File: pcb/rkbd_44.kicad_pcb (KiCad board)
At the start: 2 copper layers, 104 parts, among them SW1 SW_Push, U1 ATmega32U4-AU, Y1 16MHz

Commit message: footprint layout
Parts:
- C1, C2, D1, D10, D11, D12, D13, D14, D15, D16, D17, D18, D19, D2, D20, D21, D22, D23, D24, D25, D26, D27, D28, D29, D3, D30, D31, D32, D33, D34, D35, D36, D37, D38, D39, D4, D40, D41, D42, D43, D44, D5, D6, D7, D8, D9, R2, R3, U1, USB1, Y1: moved to B.Cu
- moved D38 245.2 mm to (276.2, 114.3)
- moved MX38 227.4 mm to (269.1, 107.2)
- moved D25 225.6 mm to (276.2, 95.2)
- moved D37 219.8 mm to (257.2, 114.3)
- moved F1 206.1 mm to (129.9, -5.09)
- moved C3 206.1 mm to (140.0, -3.07)
- moved C4 206.1 mm to (153.3, -9.42)
- moved C5 206.1 mm to (144.7, -3.07)
- moved C7 206.1 mm to (153.3, -6.47)
- moved R4 206.1 mm to (149.3, -3.07)
- moved D24 201.4 mm to (257.2, 95.2)
- moved D12 195.5 mm to (276.2, 76.2)
- moved D36 195.2 mm to (238.1, 114.3)
- moved C6 194.7 mm to (171.4, 9.53)
- moved MX35 190.0 mm to (211.9, 107.2)
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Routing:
- net col12: track 0.00 -> 138.0 mm, vias 0 -> 4
- net row2: track 0.00 -> 131.4 mm
- net row1: track 0.00 -> 131.3 mm
- net col11: track 0.00 -> 119.0 mm, vias 0 -> 4
- net row0: track 0.00 -> 105.1 mm
- net col9: track 0.00 -> 104.0 mm, vias 0 -> 6
- net col10: track 0.00 -> 99.9 mm, vias 0 -> 4
- net col8: track 0.00 -> 85.4 mm, vias 0 -> 6
- net col7: track 0.00 -> 67.0 mm, vias 0 -> 6
- net row3: track 0.00 -> 44.6 mm
- net Net-(D41-Pad2): track 0.00 -> 14.4 mm
- net Net-(D34-Pad2): track 0.00 -> 13.5 mm
- net Net-(D9-Pad2): track 0.00 -> 13.4 mm
- net Net-(D8-Pad2): track 0.00 -> 13.4 mm
- net Net-(D7-Pad2): track 0.00 -> 13.4 mm
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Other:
- board outline added: 263.3 x 90.4 mm

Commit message: change mcu position, change sw footprint
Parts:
- C3, C4, C5, C6, C7, F1, R1, R4, SW1: moved to B.Cu
- MX1, MX10, MX11, MX12, MX13, MX14, MX15, MX16, MX17, MX18, MX19, MX2, MX20, MX21, MX22, MX23, MX24, MX25, MX26, MX27, MX28, MX29, MX3, MX30, MX31, MX32, MX33, MX34, MX35, MX36, MX37, MX38, MX39, MX4, MX40, MX43, MX44, MX5, MX6, MX7, MX8, MX9: footprint MX_Only:MXOnly-1U-Hotswap -> MX_Only:MXOnly-1U-NoLED
- MX41, MX42: footprint MX_Only:MXOnly-1.25U-Hotswap -> MX_Only:MXOnly-1.25U-NoLED
- moved C7 93.3 mm to (161.0, 86.5), turned to 90 degrees
- moved C4 90.8 mm to (138.0, 80.1), turned to 90 degrees
- moved R4 88.7 mm to (139.0, 85.1)
- moved C5 80.2 mm to (163.0, 75.1), turned to 270 degrees
- moved C6 75.9 mm to (163.6, 85.1), turned to 90 degrees
- moved F1 75.5 mm to (144.0, 69.1), turned to 90 degrees
- moved C3 72.5 mm to (154.0, 68.1), turned to 90 degrees
- moved C2 28.3 mm to (165.0, 62.1), turned to 90 degrees
- moved Y1 21.7 mm to (161.0, 62.1), turned to 0 degrees
- moved C1 16.1 mm to (157.0, 62.1), turned to 270 degrees
- moved USB1 14.2 mm to (150.0, 59.5)
- moved R2 13.4 mm to (150.6, 68.1), turned to 90 degrees
- moved R3 13.3 mm to (148.6, 68.1), turned to 90 degrees
- moved R1 12.8 mm to (140.0, 68.1), turned to 270 degrees
- moved U1 7.20 mm to (152.0, 78.1), turned to 270 degrees
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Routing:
- net col7: track 67.0 -> 0.00 mm, vias 6 -> 0
- net row3: track 44.6 -> 0.00 mm
- net col8: track 85.4 -> 61.1 mm
- net Net-(D41-Pad2): track 14.4 -> 0.00 mm
- net Net-(D7-Pad2): track 13.4 -> 0.00 mm
- net Net-(D33-Pad2): track 13.4 -> 0.00 mm
- net Net-(D20-Pad2): track 13.3 -> 0.00 mm
- net col9: track 104.0 -> 91.3 mm
- net col10: track 99.9 -> 87.9 mm
- net col11: track 119.0 -> 109.0 mm
- net col12: track 138.0 -> 128.4 mm
- net row2: track 131.4 -> 125.0 mm
- net row1: track 131.3 -> 125.5 mm
- net row0: track 105.1 -> 100.9 mm
- net Net-(D37-Pad2): track 13.4 -> 16.7 mm
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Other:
- board outline removed

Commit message: add cutting line
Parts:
- moved C1 20.6 mm to (165.0, 81.1), turned to 0 degrees
- moved C6 17.0 mm to (158.0, 69.1), turned to 180 degrees
- moved Y1 15.5 mm to (165.0, 77.1), turned to 90 degrees
- moved C2 11.0 mm to (165.0, 73.1), turned to 180 degrees
- moved C4 6.12 mm to (143.4, 82.9), turned to 180 degrees
- moved C5 2.83 mm to (161.0, 73.1)
- moved C7 1.22 mm to (161.9, 85.7), turned to 0 degrees
- turned D1 to 0 degrees
- turned D13 to 0 degrees
- turned D14 to 0 degrees
- turned D15 to 0 degrees
- turned D16 to 0 degrees
- turned D17 to 0 degrees
- turned D18 to 0 degrees
- turned D2 to 0 degrees
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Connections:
- U1 pad 18: Net-(U1-Pad18) -> row0
- U1 pad 19: Net-(U1-Pad19) -> col12
- U1 pad 20: Net-(U1-Pad20) -> col11
- U1 pad 21: Net-(U1-Pad21) -> col10
- U1 pad 22: Net-(U1-Pad22) -> col9
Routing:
- net row3: track 0.00 -> 108.6 mm
- net GND: track 0.00 -> 93.1 mm
- net col7: track 0.00 -> 62.1 mm, vias 0 -> 6
- net +5V: track 0.00 -> 34.6 mm
- net Net-(R1-Pad1): track 0.00 -> 31.9 mm, vias 0 -> 2
- net row0: track 100.9 -> 126.7 mm
- net col11: track 109.0 -> 134.1 mm
- net col12: track 128.4 -> 153.4 mm
- net col9: track 91.3 -> 116.3 mm
- net col8: track 61.1 -> 86.0 mm
- net col10: track 87.9 -> 112.8 mm
- net row1: track 125.5 -> 146.0 mm
- net col6: track 0.00 -> 18.7 mm, vias 0 -> 2
- net Net-(C2-Pad1): track 0.00 -> 16.5 mm, vias 0 -> 2
- net Net-(D7-Pad2): track 0.00 -> 16.4 mm
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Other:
- board outline added: 257.2 x 78.1 mm
- net class Power added: clearance 0.2, trace_width 0.381, via_dia 0.8, via_drill 0.4

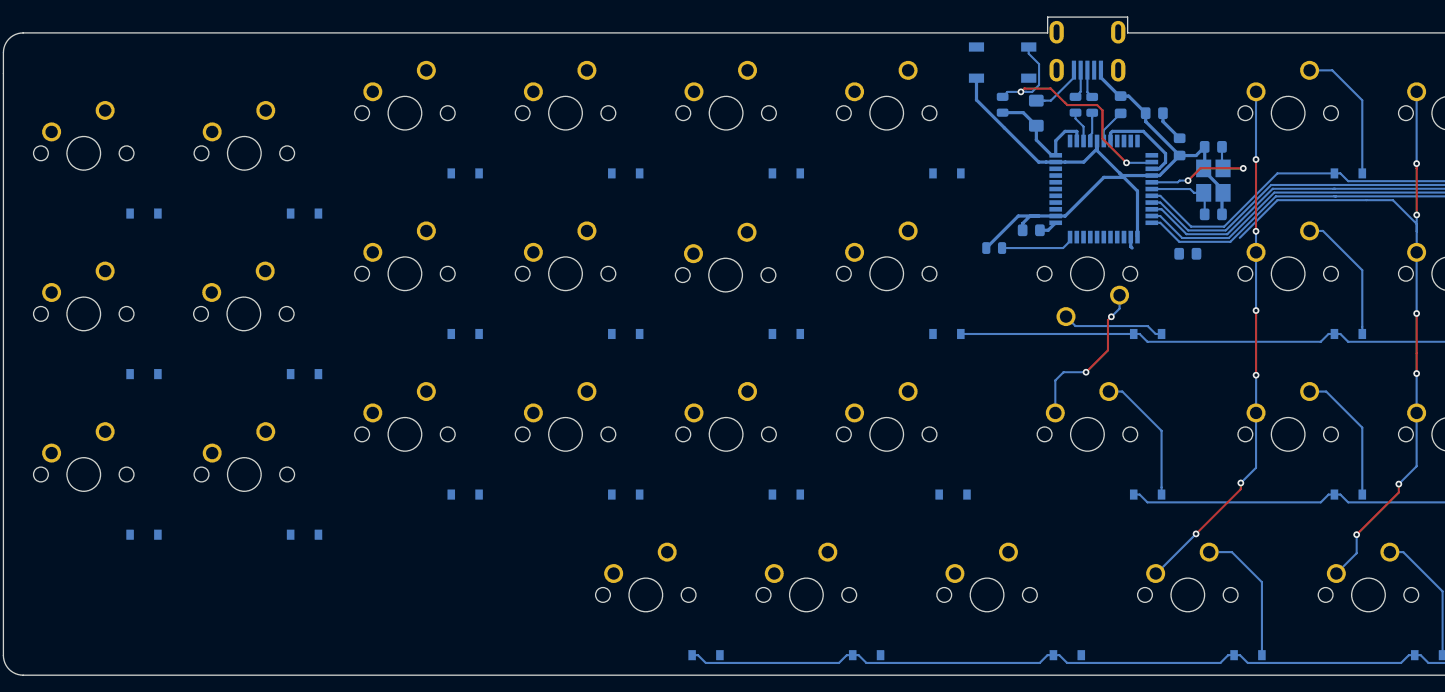
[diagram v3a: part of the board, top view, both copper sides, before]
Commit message: Routing all, Ground fills
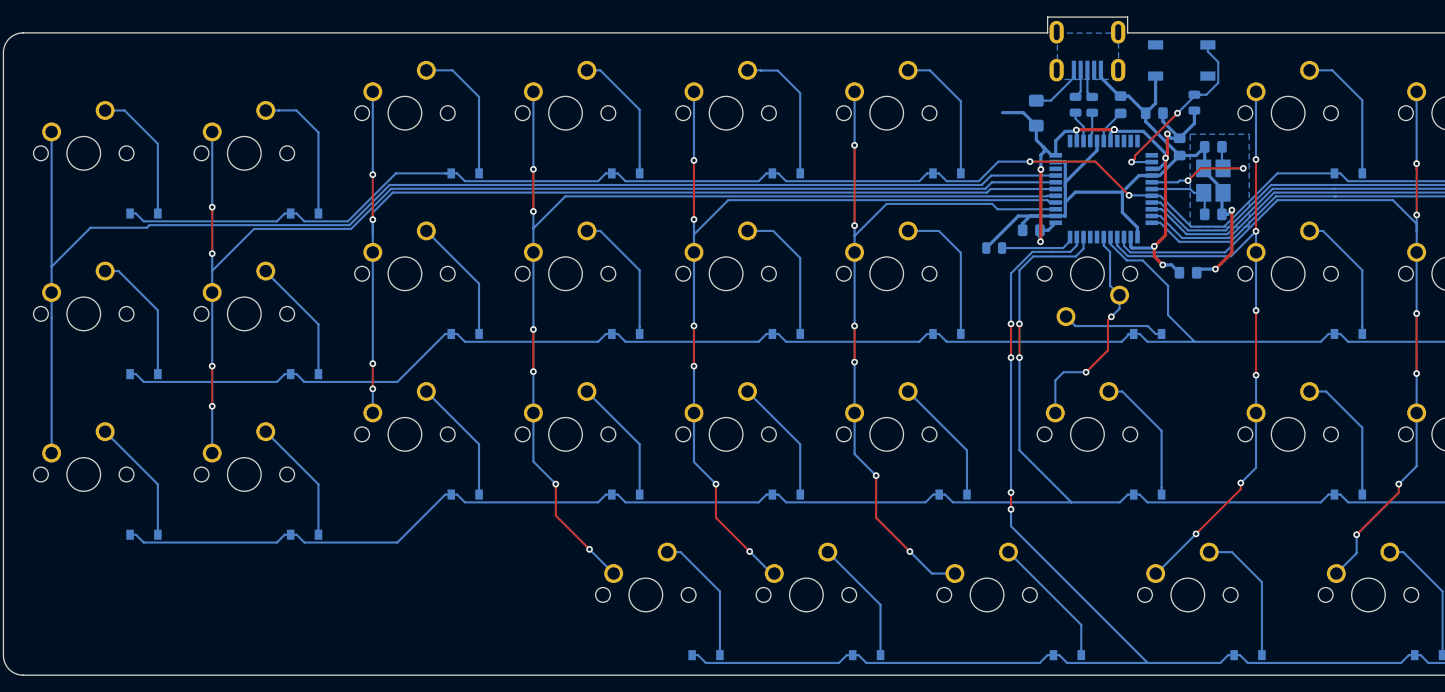
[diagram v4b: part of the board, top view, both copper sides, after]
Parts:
- moved R1 22.8 mm to (162.7, 67.8)
- moved SW1 21.3 mm to (161.2, 62.8)
- moved C7 2.25 mm to (162.0, 88.0)
- moved MX17 0.17 mm to (107.2, 88.1)
- moved MX14 0.06 mm to (50.0, 92.9)
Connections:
- U1 pad 25: Net-(U1-Pad25) -> col8
- U1 pad 26: Net-(U1-Pad26) -> col7
- U1 pad 27: Net-(U1-Pad27) -> row1
- U1 pad 28: Net-(U1-Pad28) -> col6
- U1 pad 31: Net-(U1-Pad31) -> row2
- U1 pad 32: Net-(U1-Pad32) -> row3
- U1 pad 36: Net-(U1-Pad36) -> col5
- U1 pad 37: Net-(U1-Pad37) -> col4
- U1 pad 38: Net-(U1-Pad38) -> col3
- U1 pad 39: Net-(U1-Pad39) -> col2
- U1 pad 40: Net-(U1-Pad40) -> col1
- U1 pad 41: Net-(U1-Pad41) -> col0
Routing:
- net row2: track 125.0 -> 290.8 mm, vias 0 -> 2
- net col0: track 0.00 -> 161.7 mm
- net col1: track 0.00 -> 142.7 mm, vias 0 -> 4
- net row0: track 126.7 -> 257.4 mm, vias 0 -> 2
- net col3: track 0.00 -> 124.7 mm, vias 0 -> 6
- net row1: track 146.0 -> 268.9 mm
- net col2: track 0.00 -> 122.9 mm, vias 0 -> 4
- net col4: track 0.00 -> 106.0 mm, vias 0 -> 6
- net col5: track 0.00 -> 89.4 mm, vias 0 -> 6
- net row3: track 108.6 -> 171.7 mm, vias 0 -> 4
- net +5V: track 34.6 -> 80.0 mm, vias 0 -> 9
- net col7: track 62.1 -> 81.4 mm
- net Net-(D2-Pad2): track 0.00 -> 17.0 mm
- net Net-(D18-Pad2): track 0.00 -> 17.0 mm
- net Net-(D5-Pad2): track 0.00 -> 16.9 mm
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- added copper zone on B.Cu, net GND

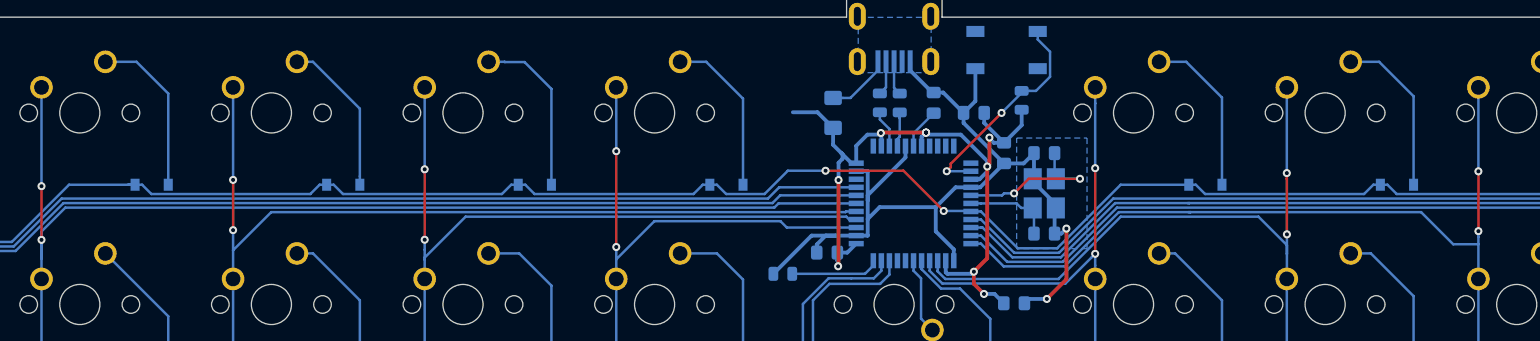
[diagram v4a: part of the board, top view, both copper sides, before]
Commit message: fix mcu routing
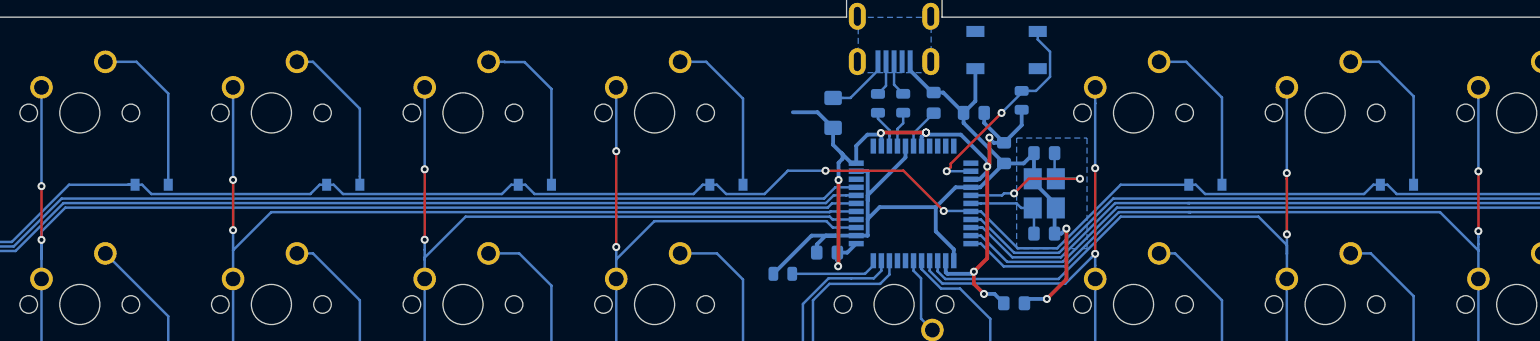
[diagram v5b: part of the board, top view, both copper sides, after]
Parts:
- moved R2 0.35 mm to (150.9, 68.1)
- moved R3 0.20 mm to (148.4, 68.1)

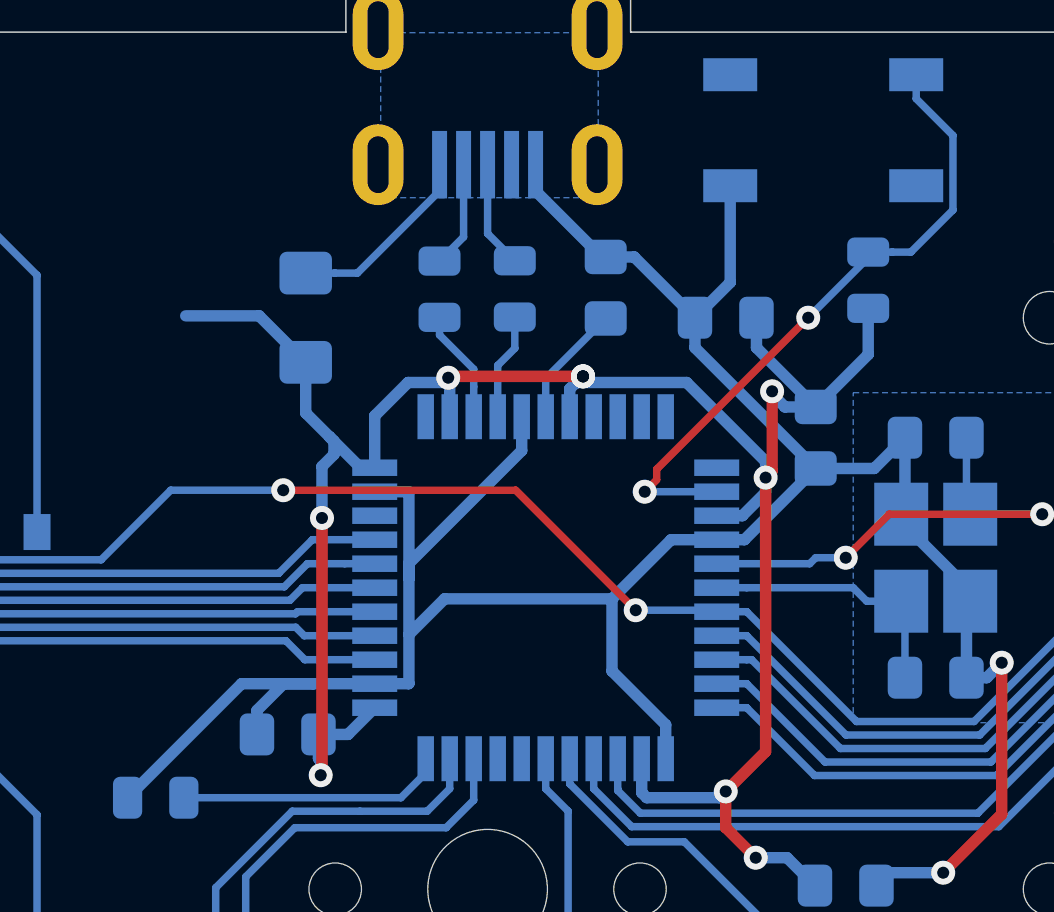
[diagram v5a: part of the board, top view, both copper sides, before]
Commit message: Fill zones, fix drc erro
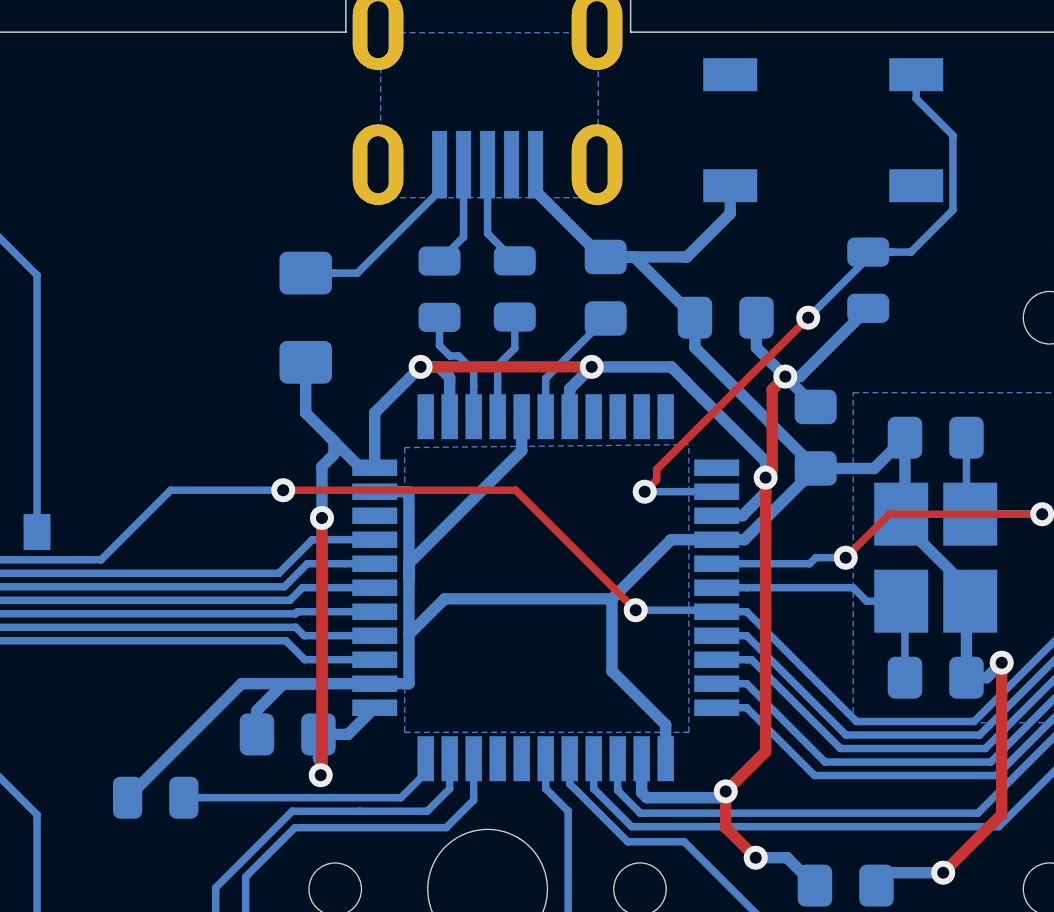
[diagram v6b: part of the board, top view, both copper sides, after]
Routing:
- net +5V: track 80.0 -> 75.7 mm, vias 9 -> 8
- net GND: track 94.0 -> 94.8 mm

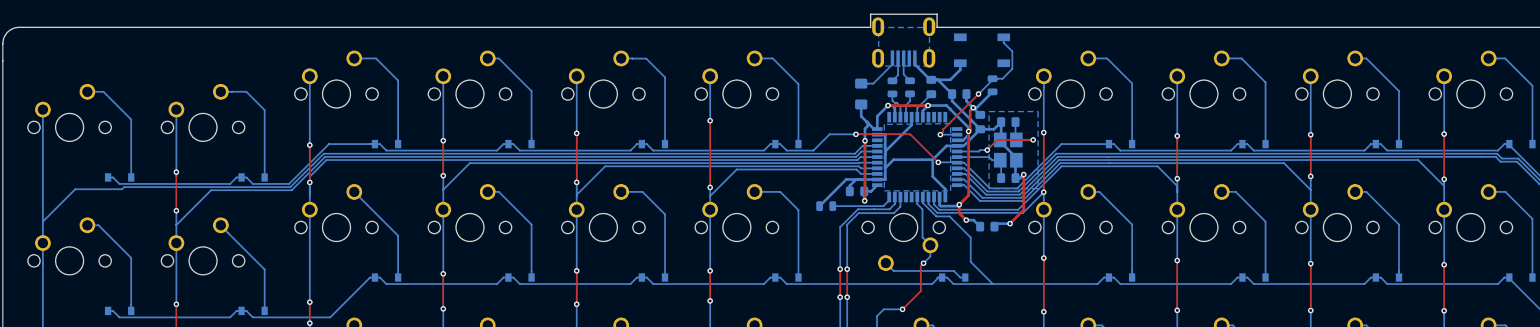
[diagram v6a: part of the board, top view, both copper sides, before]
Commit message: mcu change promicro
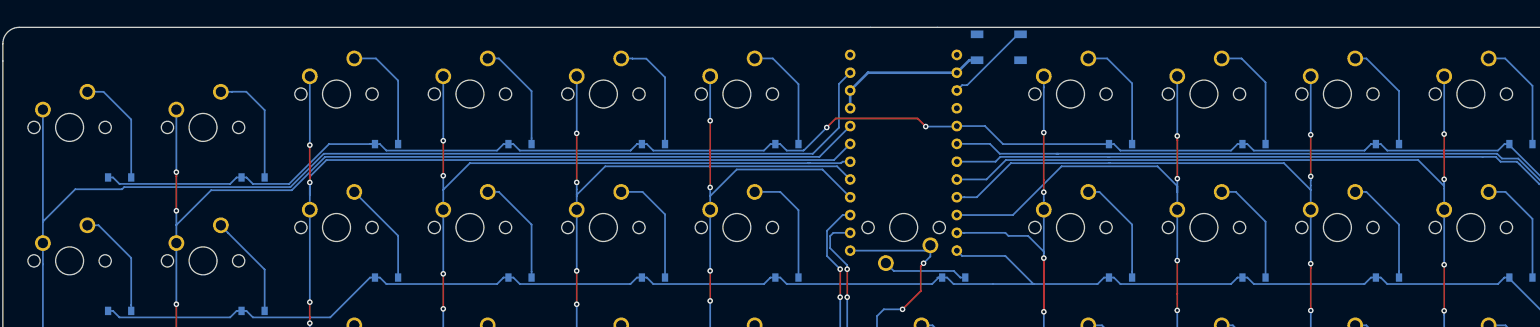
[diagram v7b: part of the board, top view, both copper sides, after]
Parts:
- removed C1, C2: 22pF, Capacitor_SMD:C_0805_2012Metric_Pad1.15x1.40mm_HandSolder
- removed C3: 1uF, Capacitor_SMD:C_0805_2012Metric_Pad1.15x1.40mm_HandSolder
- removed C4, C5, C6: 0.1uF, Capacitor_SMD:C_0805_2012Metric_Pad1.15x1.40mm_HandSolder
- removed C7: 10uF, Capacitor_SMD:C_0805_2012Metric_Pad1.15x1.40mm_HandSolder
- removed F1: 500mA, Fuse:Fuse_1206_3216Metric_Pad1.42x1.75mm_HandSolder
- removed R1, R4: 10k, Resistor_SMD:R_0805_2012Metric
- removed R2, R3: 22, Resistor_SMD:R_0805_2012Metric
- removed USB1: Molex-0548190589, random-keyboard-parts:Molex-0548190589
- removed Y1: 16MHz, Crystal:Crystal_SMD_3225-4Pin_3.2x2.5mm_HandSoldering
- U1: value ATmega32U4-AU -> ProMicro; footprint Package_QFP:TQFP-44_10x10mm_P0.8mm -> kbd:ProMicro_v3.5
- moved SW1 2.43 mm to (163.6, 62.4), turned to 0 degrees
- moved U1 1.96 mm to (150.0, 77.9), turned to 180 degrees
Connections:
- SW1 pad 1: GND -> RSET
- SW1 pad 2: Net-(R1-Pad1) -> GND
- U1 pad 10: Net-(U1-Pad10) -> row3
- U1 pad 11: Net-(U1-Pad11) -> row2
- U1 pad 12: Net-(U1-Pad12) -> col6
- U1 pad 13: Net-(R1-Pad1) -> row1
- U1 pad 14: +5V -> col7
- U1 pad 15: GND -> col8
- U1 pad 16: Net-(C2-Pad1) -> col9
- U1 pad 17: Net-(C1-Pad1) -> col10
- U1 pad 18: row0 -> col11
- U1 pad 2: +5V -> col0
- U1 pad 20: col11 -> row0
- U1 pad 21: col10 -> VCC
- U1 pad 22: col9 -> RSET
- U1 pad 24: +5V -> Net-(U1-Pad24)
- U1 pad 3: Net-(R3-Pad1) -> GND
- U1 pad 4: Net-(R2-Pad1) -> GND
- U1 pad 5: GND -> col1
- U1 pad 6: Net-(C3-Pad1) -> col2
- U1 pad 7: +5V -> col3
- U1 pad 8: Net-(U1-Pad8) -> col4
- U1 pad 9: Net-(U1-Pad9) -> col5
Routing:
- net +5V: track 75.7 -> 0.00 mm, vias 8 -> 0
- net GND: track 94.8 -> 22.4 mm, vias 2 -> 0
- net Net-(R1-Pad1): track 22.0 -> 0.00 mm, vias 2 -> 0
- net Net-(C2-Pad1): track 16.5 -> 0.00 mm, vias 2 -> 0
- net RSET: track 0.00 -> 12.4 mm
- net Net-(C1-Pad1): track 8.94 -> 0.00 mm
- net Net-(R4-Pad2): track 8.88 -> 0.00 mm
- net row2: track 290.8 -> 283.2 mm
- net VCC: track 6.47 -> 0.00 mm
- net col7: track 81.4 -> 75.7 mm
- net row3: track 171.7 -> 166.1 mm
- net row1: track 268.9 -> 264.2 mm
- net col8: track 101.8 -> 97.5 mm
- net col0: track 161.7 -> 165.8 mm
- net Net-(C3-Pad1): track 4.10 -> 0.00 mm
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- removed copper zone on B.Cu, net GND
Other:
- board size 257.2 x 78.1 mm -> 257.2 x 76.2 mm
